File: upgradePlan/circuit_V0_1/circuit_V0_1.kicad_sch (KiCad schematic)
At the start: 20 parts, among them J1 Connector_GY_521, M1 Motor_DC, M2 Motor_Servo, SW1 SW_DIP_x01, U1 Freenove-SP32-WROVER, U2 L293D, U3 LM317_TO-220, U5 LM317_TO-220

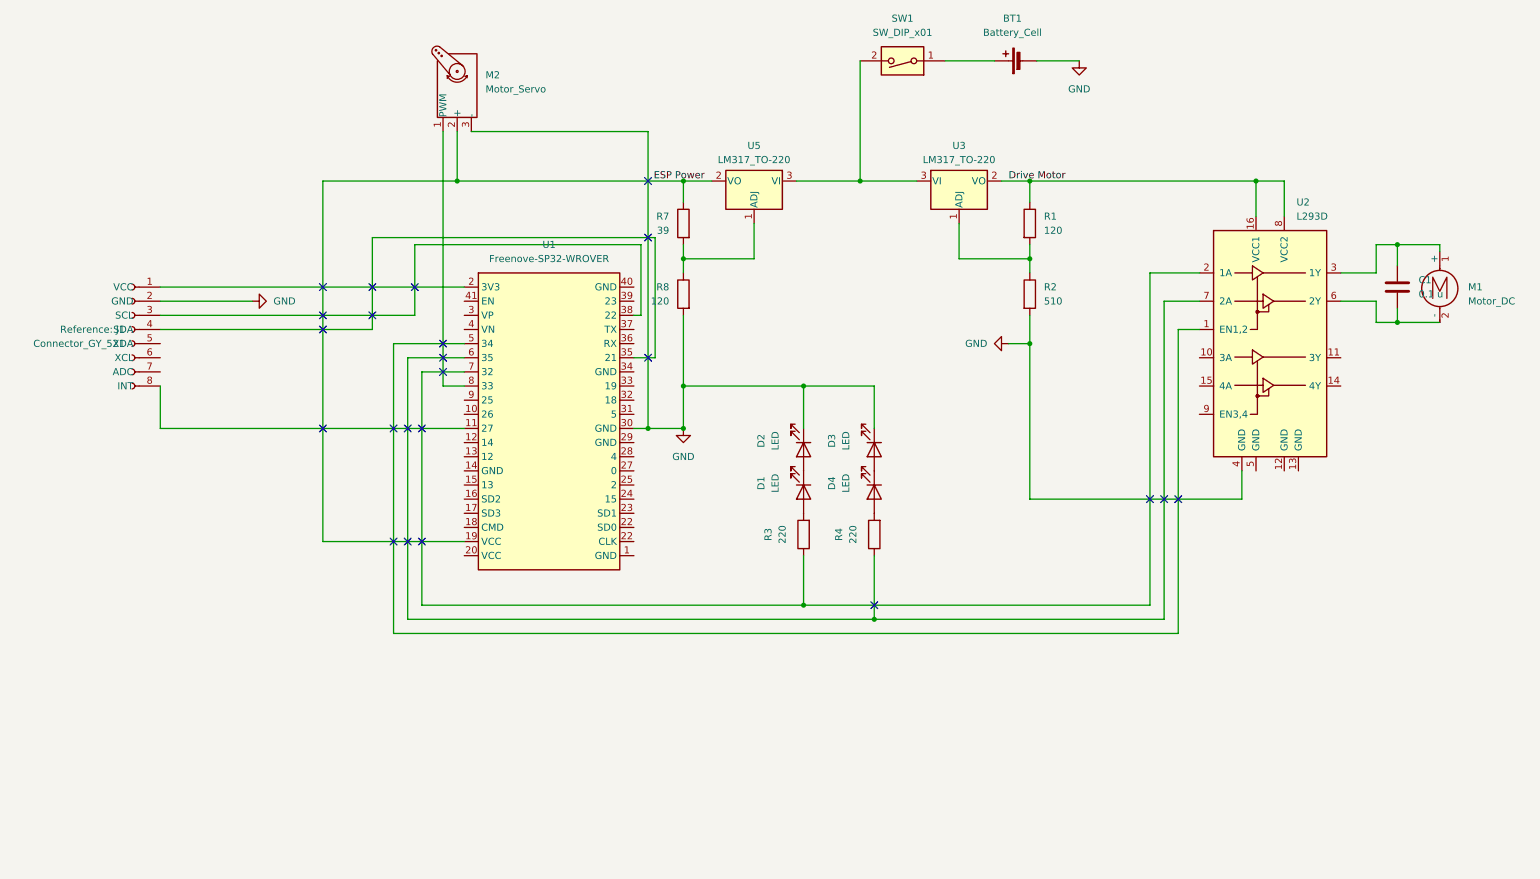
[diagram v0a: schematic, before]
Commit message: Changed the circuit and added struct for custom messages
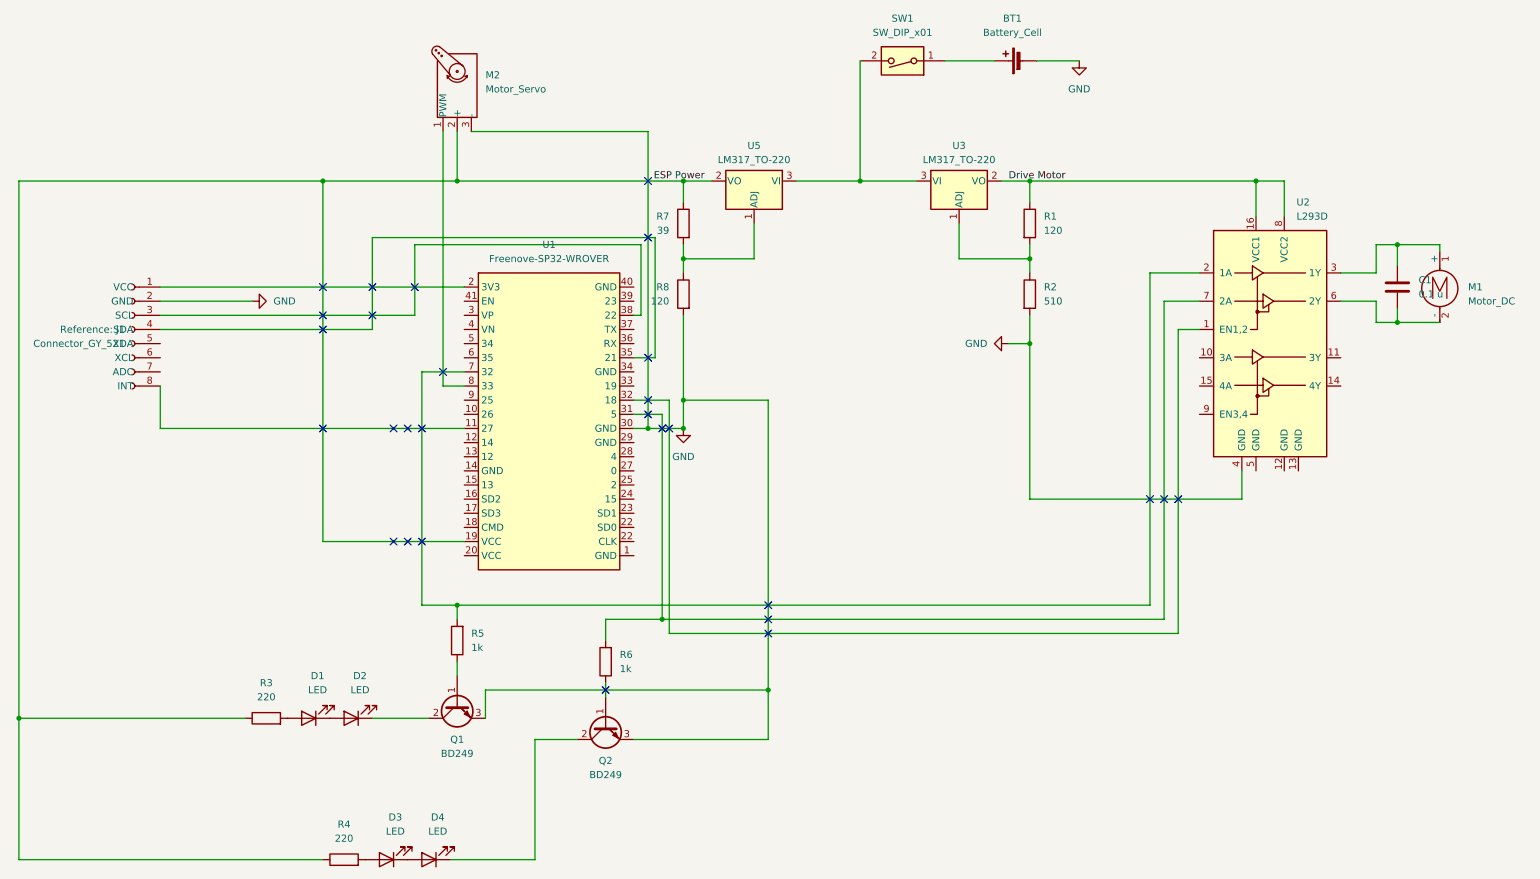
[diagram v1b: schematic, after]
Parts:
- added Q1, Q2: BD249, symbol Transistor_BJT:BD249
- added R5, R6: 1k, symbol Device:R
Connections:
- net ESP Power: now also R3.1, R4.1
- net GND: now also Q1.3 (E), Q2.3 (E); no longer D2.1 (K), D3.1 (K)
- net at D3.2 (A): now also R4.2; no longer D4.1 (K)
- net at D4.2 (A): now also D3.1 (K); no longer R4.2
- net at U1.31 (5): now also U2.7 (2A), R6.2
- net at U1.32 (18): now also U2.1 (EN1,2)
- net at U1.5 (34): no longer U2.1 (EN1,2)
- net at U1.7 (32), U2.2 (1A): now also R5.2; no longer R3.1
- new net: Q1.1 (B), R5.1
- new net: D2.1 (K), Q1.2 (C)
- new net: D4.1 (K), Q2.2 (C)
- new net: Q2.1 (B), R6.1
- now unconnected: U1.6 (35)
- no-connect marks 23 -> 28
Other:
- moved on the sheet: D1, D2, R3

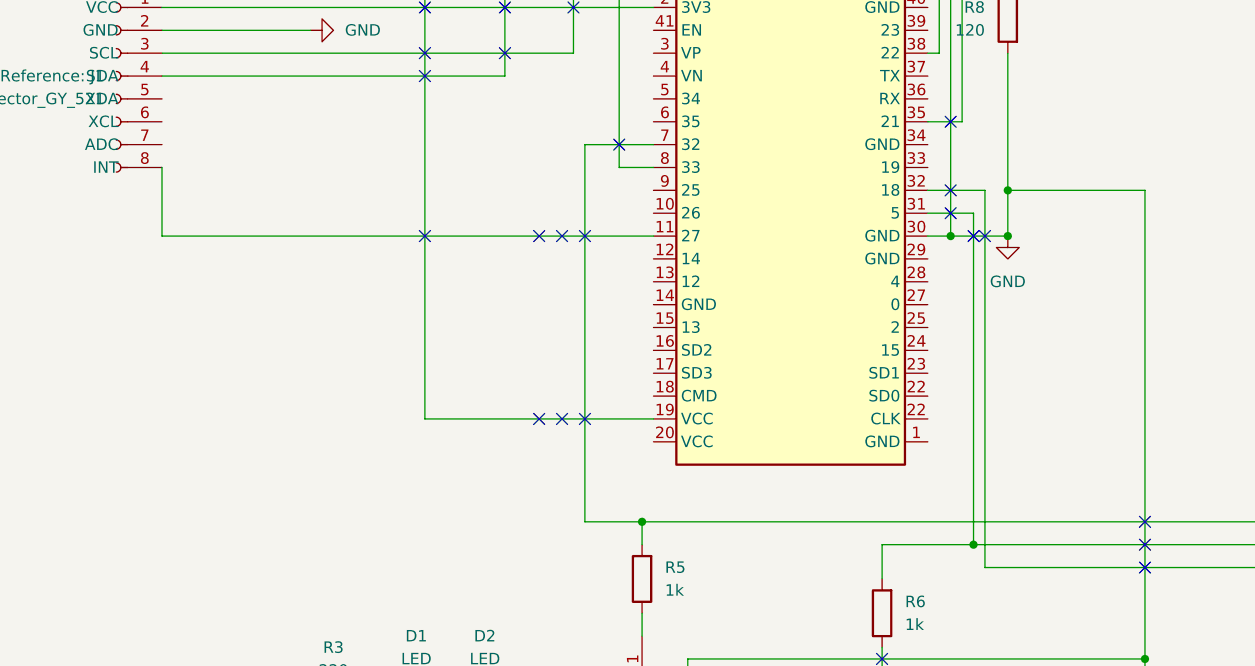
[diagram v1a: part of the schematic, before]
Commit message: created the publisher for the accelerometer created the setup for the mpu6050
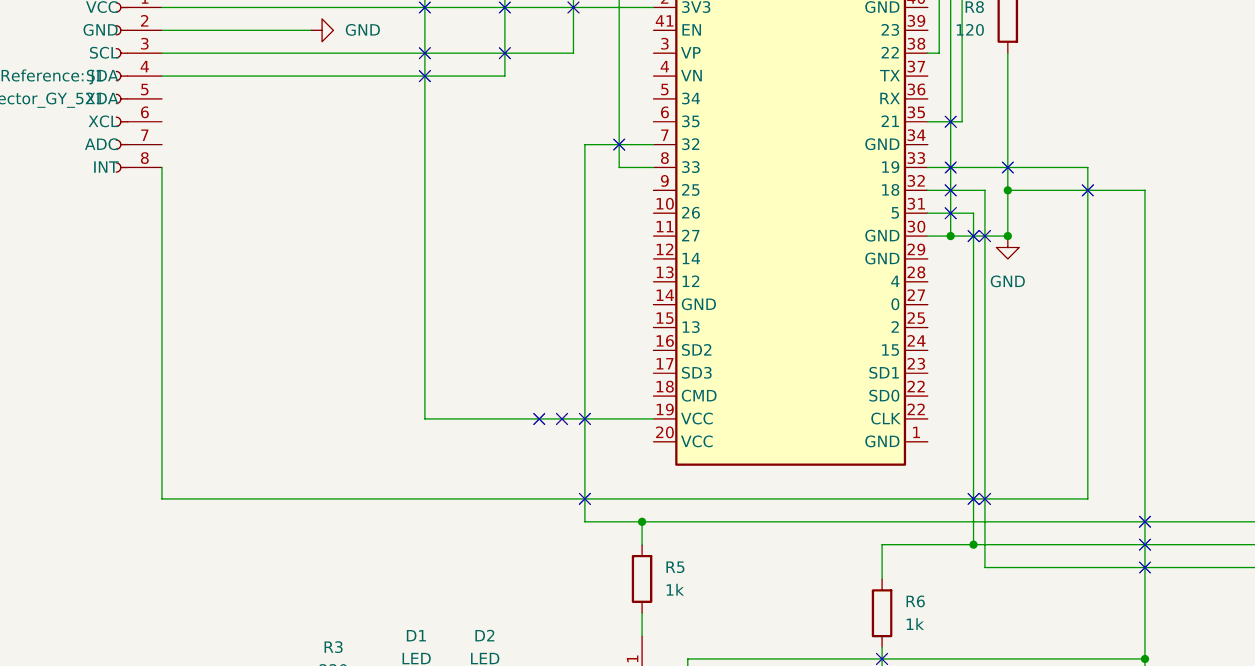
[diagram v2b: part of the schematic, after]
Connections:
- net at J1.8 (INT): now also U1.33 (19); no longer U1.11 (27)
- no-connect marks 28 -> 30
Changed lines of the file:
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@@
   (no_connect (at 82.55 71.12))
   (no_connect (at 95.25 81.28))
+  (no_connect (at 91.44 120.65))
   (no_connect (at 134.62 91.44))
   (no_connect (at 124.46 138.43))
@@
   (no_connect (at 73.66 73.66))
   (no_connect (at 153.67 128.27))
+  (no_connect (at 134.62 120.65))
   (no_connect (at 132.08 86.36))
   (no_connect (at 222.25 104.14))
-  (no_connect (at 73.66 91.44))
   (no_connect (at 73.66 66.04))
+  (no_connect (at 135.89 120.65))
   (no_connect (at 82.55 66.04))
   (no_connect (at 90.17 66.04))
   (no_connect (at 91.44 111.76))
-  (no_connect (at 86.36 91.44))
   (no_connect (at 135.89 91.44))
+  (no_connect (at 147.32 86.36))
   (no_connect (at 86.36 111.76))
-  (no_connect (at 88.9 91.44))
   (no_connect (at 73.66 71.12))
   (no_connect (at 88.9 111.76))
+  (no_connect (at 132.08 83.82))
   (no_connect (at 153.67 123.19))
-  (no_connect (at 91.44 91.44))
   (no_connect (at 132.08 78.74))
   (no_connect (at 132.08 57.15))
   (no_connect (at 132.08 88.9))
+  (no_connect (at 138.43 83.82))
   (wire (pts (xy 132.08 38.1) (xy 132.08 91.44))
     (stroke (width 0) (type default))
@@
     (stroke (width 0) (type default))
   )
-  (wire (pts (xy 44.45 91.44) (xy 44.45 83.82))
+  (wire (pts (xy 44.45 83.82) (xy 44.45 120.65))
     (stroke (width 0) (type default))
   )
@@
     (stroke (width 0) (type default))
   )
+  (wire (pts (xy 129.54 83.82) (xy 147.32 83.82))
+    (stroke (width 0) (type default))
+  )
   (wire (pts (xy 151.13 54.61) (xy 151.13 60.96))
     (stroke (width 0) (type default))
@@
     (stroke (width 0) (type default))
   )
+  (wire (pts (xy 147.32 120.65) (xy 147.32 83.82))
+    (stroke (width 0) (type default))
+  )
   (wire (pts (xy 256.54 68.58) (xy 262.89 68.58))
     (stroke (width 0) (type default))
@@
     (stroke (width 0) (type default))
   )
+  (wire (pts (xy 44.45 120.65) (xy 147.32 120.65))
+    (stroke (width 0) (type default))
+  )
   (wire (pts (xy 44.45 68.58) (xy 60.96 68.58))
     (stroke (width 0) (type default))
@@
     (stroke (width 0) (type default))
   )
-  (wire (pts (xy 99.06 91.44) (xy 44.45 91.44))
-    (stroke (width 0) (type default))
-  )
